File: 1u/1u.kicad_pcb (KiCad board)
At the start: 2 copper layers, 19.1 x 19 mm, 28 parts, among them J1 Conn_01x01_Pin, J10 Conn_01x01_Pin, J11 Conn_01x01_Pin, J12 Conn_01x01_Pin, J13 Conn_01x01_Pin, J14 Conn_01x01_Pin, J2 Conn_01x01_Pin, J3 Conn_01x01_Pin, J4 Conn_01x01_Pin, J5 Conn_01x01_Pin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

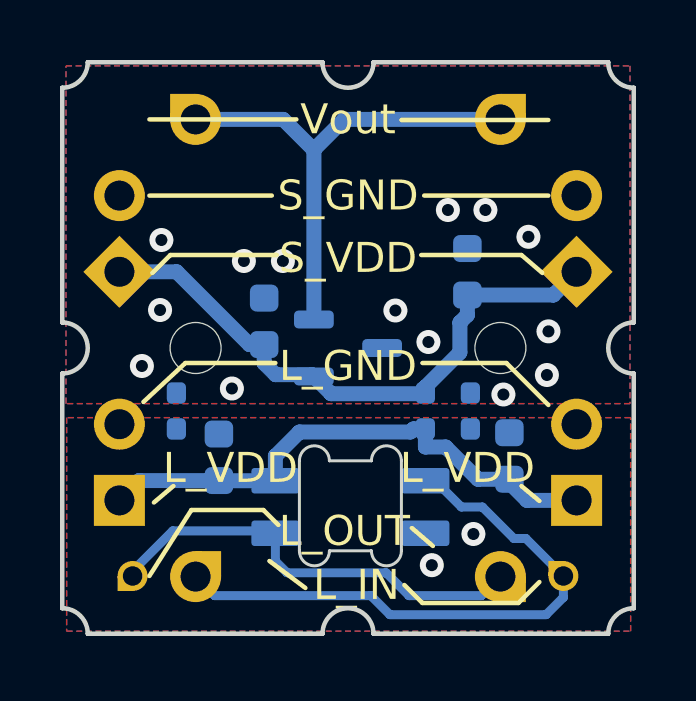
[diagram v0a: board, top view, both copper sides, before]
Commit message: fixes silkscreen
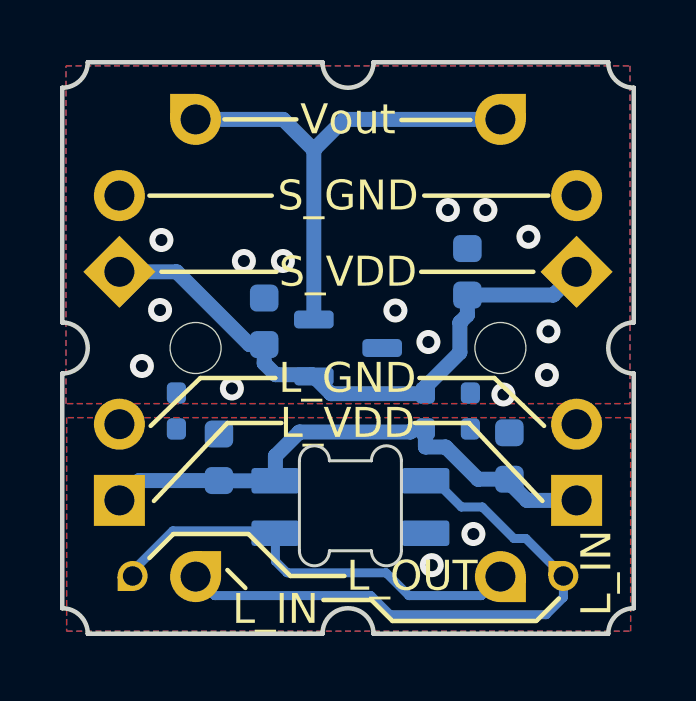
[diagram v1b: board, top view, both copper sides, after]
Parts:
- removed REF** (x4): Tab, kikit:Tab
